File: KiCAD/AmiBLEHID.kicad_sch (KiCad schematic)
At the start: 10 parts, among them J1 D-Sub Female, SW1 Reset, SW2 Mode, U1 ESP32-H2-Zero, U2 74HC05

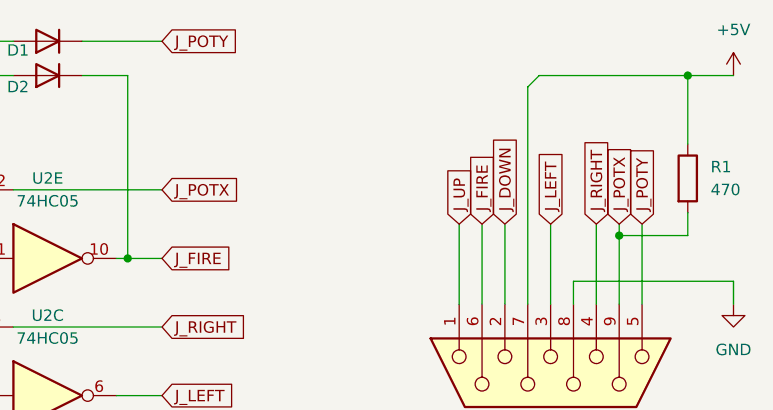
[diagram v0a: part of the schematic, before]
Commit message: v0.5 PCB layout, more compact design to fit A600
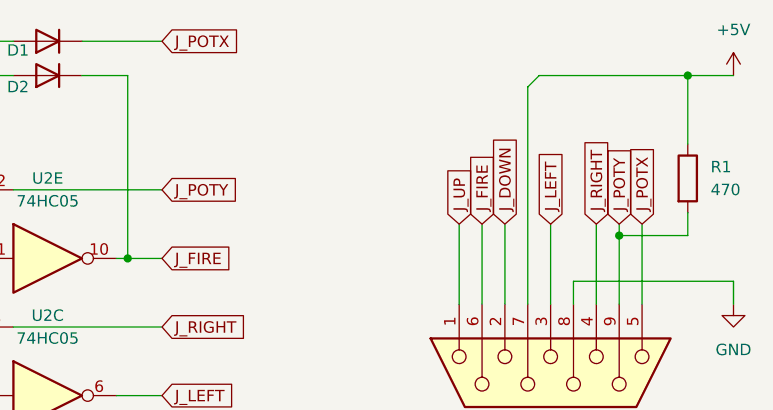
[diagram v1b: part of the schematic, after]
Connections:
- net J_POTX: now also D1.1 (K), J1.5; no longer J1.9, R1.2, U2.12
- net J_POTY: now also J1.9, R1.2, U2.12; no longer D1.1 (K), J1.5
